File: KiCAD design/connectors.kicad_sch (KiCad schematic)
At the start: 8 parts, among them J201 Conn_02x19_Odd_Even, J202 Conn_01x03_Female, J203 Conn_01x03_Female, J204 Conn_02x19_Odd_Even, J205 JST BATTERY, J206 JST SENS TOF 2, J208 JST SENS TOF 1, J401 Conn_02x06_Top_Bottom

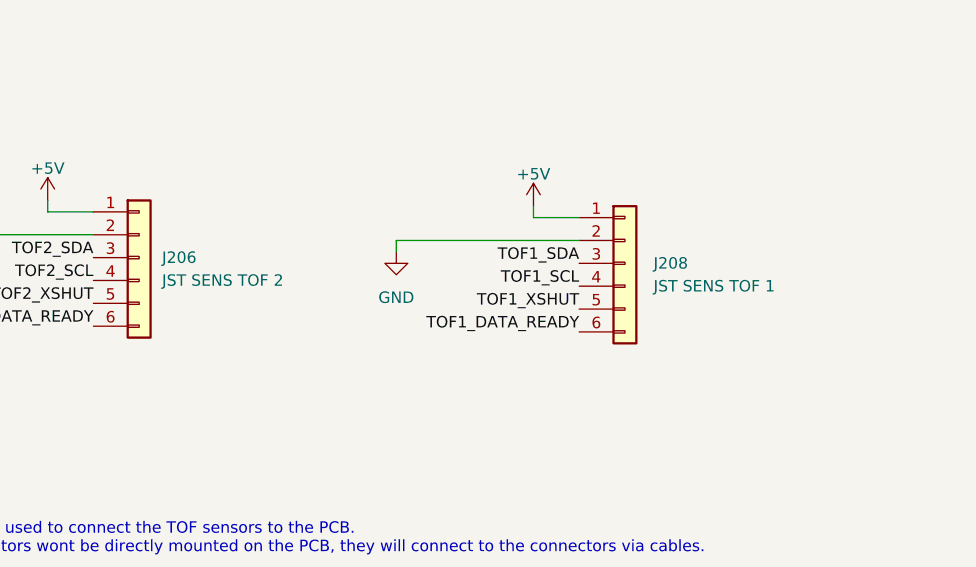
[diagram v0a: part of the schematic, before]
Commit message: set same value for TOF sensor connectors to group them in BOM
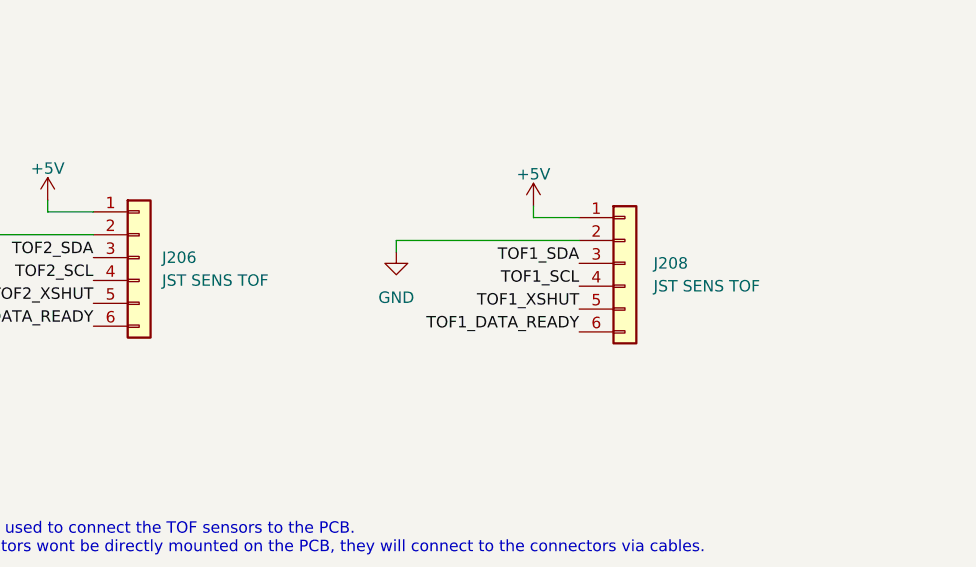
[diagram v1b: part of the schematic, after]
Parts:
- J206: value JST SENS TOF 2 -> JST SENS TOF
- J208: value JST SENS TOF 1 -> JST SENS TOF
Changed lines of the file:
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@@
       (effects (font (size 1.27 1.27)) (justify left))
     )
-    (property "Value" "JST SENS TOF 2" (id 1) (at 205.74 60.9599 0)
+    (property "Value" "JST SENS TOF" (id 1) (at 205.74 60.9599 0)
       (effects (font (size 1.27 1.27)) (justify left))
     )
@@
       (effects (font (size 1.27 1.27)) (justify left))
     )
-    (property "Value" "JST SENS TOF 1" (id 1) (at 260.35 61.5949 0)
+    (property "Value" "JST SENS TOF" (id 1) (at 260.35 61.5949 0)
       (effects (font (size 1.27 1.27)) (justify left))
     )

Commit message: end PCB
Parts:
- J206: value JST SENS TOF -> JST SENS TOF 2
- J208: value JST SENS TOF -> JST SENS TOF 1
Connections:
- net RST_N is gone; now on net +3.3V: J401.8 (Pin_8)
- net BT_3.3V: now reaches J201.16 (Pin_16)
- no-connect marks 16 -> 15
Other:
- moved on the sheet: J401

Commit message: tof sensor values and lipo bat
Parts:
- J206: value JST SENS TOF 2 -> JST SENS TOF
- J208: value JST SENS TOF 1 -> JST SENS TOF
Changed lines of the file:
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@@
       (effects (font (size 1.27 1.27)) (justify left))
     )
-    (property "Value" "JST SENS TOF 2" (id 1) (at 205.74 60.9599 0)
+    (property "Value" "JST SENS TOF" (id 1) (at 205.74 60.9599 0)
       (effects (font (size 1.27 1.27)) (justify left))
     )
@@
       (effects (font (size 1.27 1.27)) (justify left))
     )
-    (property "Value" "JST SENS TOF 1" (id 1) (at 260.35 61.5949 0)
+    (property "Value" "JST SENS TOF" (id 1) (at 260.35 61.5949 0)
       (effects (font (size 1.27 1.27)) (justify left))
     )
